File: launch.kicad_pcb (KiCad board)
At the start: 4 copper layers, 299 x 127 mm, 356 parts, among them J0 12401598E4#2A, J1 AVR-ISP-6, J2 1003-002-01100, J3 1003-002-01100, J4 12401598E4#2A, J5 12401598E4#2A, U0 USBLC6-2SC6, U1 ATmega32U4-MU, U10 AP22811AW5-7, U11 PTN5110DHQ, U12 PTN5110THQ, U13 PTN5110THQ, U14 SN74LVC1G08DCKR, U15 CBTL02043ABQ,115, U16 AP22811AW5-7‎, U17 TLV62585PDRLR, U18 LP5907MFX-3.3, U19 SN74LVC1G08DCKR, U2 USB7206, U20 AP22811AW5-7, U21 USBLC6-2SC6, U22 AP22811AW5-7, U23 AP22811AW5-7, U3 CBTL02043ABQ,115, U4 TLV62585PDRLR, U5 USBLC6-2SC6, U6 CBTL02043ABQ,115, U7 USBLC6-2SC6, U8 USBLC6-2SC6, U9 AP22811AW5-7, X1 ECS-3225MV-250-BN-TR, Y0 ECS-160-18-23G-JGN-TR

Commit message: BOM update Add manufacturer info Add key socket PN Correct USB-A to surface mount (was through hole)
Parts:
- J1: value AVR-ISP-6 -> DNP
- SWA0, SWA1, SWA2, SWA3, SWA4, SWA5, SWB0, SWB1, SWB2, SWB3, SWB4, SWB5, SWC0, SWC1, SWC2, SWC3, SWC4, SWC5, SWD0, SWD1, SWD2, SWD3, SWD4, SWD5, SWE0, SWE1, SWE2, SWE3, SWE4, SWE5, SWF0, SWF1, SWF2, SWF3, SWF4, SWF5, SWG0, SWG1, SWG2, SWG3, SWG4, SWG5, SWH0, SWH1, SWH2, SWH3, SWH4, SWH5, SWI0, SWI1, SWI2, SWI3, SWI4, SWI5, SWJ0, SWJ1, SWJ2, SWJ3, SWJ4, SWJ5, SWK0, SWK1, SWK2, SWK3, SWK4, SWK5, SWL0, SWL1, SWL2, SWL3, SWL4, SWL5, SWM0, SWM1, SWM2, SWM3, SWM4, SWM5, SWN0, SWN1, SWN2, SWN3, SWN4, SWN5: value SW_Push -> CPG151101S11
- TP1, TP2: value TestPoint -> DNP

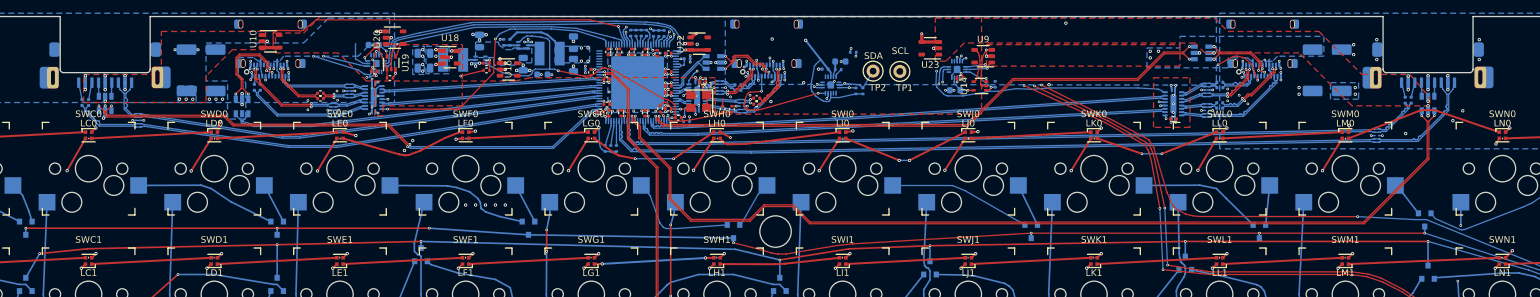
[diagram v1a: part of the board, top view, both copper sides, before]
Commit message: move USB A down 2.1 mm
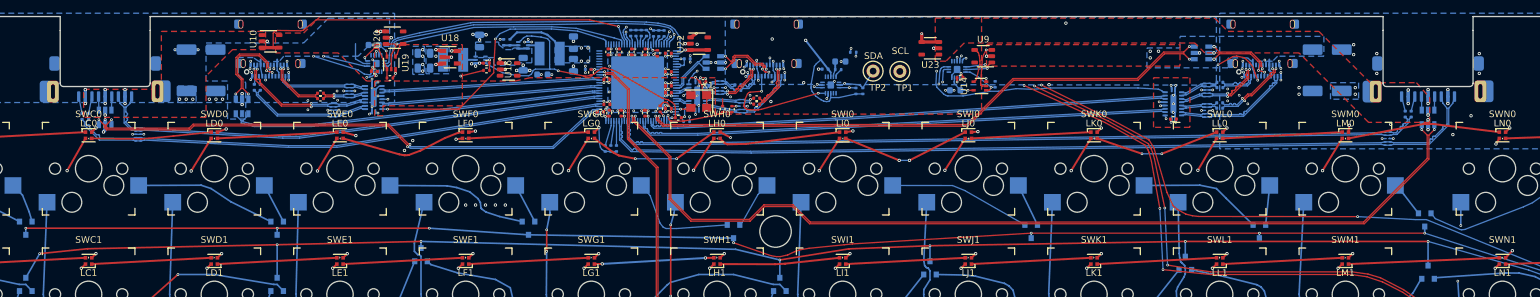
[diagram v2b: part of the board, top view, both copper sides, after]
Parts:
- moved C51 2.10 mm to (247.9, 1.75)
- moved C52 2.10 mm to (247.1, 1.75)
- moved C53 2.10 mm to (48.0, 2.10)
- moved C54 2.10 mm to (47.0, 2.10)
- moved U5 2.10 mm to (250.5, 2.25)
- moved U8 2.10 mm to (50.5, 2.25)
- moved D6 2.10 mm to (55.5, 4.80)
- moved J2 2.10 mm to (250.5, -5.90)
- moved J3 2.10 mm to (50.5, -5.90)
- moved D2 1.71 mm to (244.4, 5.45)
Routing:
- net /USB/AR_D-: track 144.7 -> 142.6 mm
- net /USB/AR_D+: track 145.6 -> 143.5 mm
- net Net-(LM0-Pad3): track 24.1 -> 23.1 mm
- net /USB/AR_RX-: track 135.4 -> 134.7 mm
- net /USB/AR_RX+: track 135.5 -> 134.7 mm
- net /USB/AR_TX-: track 123.6 -> 122.9 mm
- net /USB/AR_TX+: track 123.7 -> 123.0 mm
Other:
- outline, holes or cut-outs redrawn

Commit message: plated mounting holes adjust position of one mounting hole slightly add hole near middle.
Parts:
- added H1: MountingHole_Pad, launch:MountingHole, F.Cu at (18.9, 19.5)
- added H2: MountingHole_Pad, launch:MountingHole, F.Cu at (6.10, 105.0)
- added H3: MountingHole_Pad, launch:MountingHole, F.Cu at (30.7, 64.5)
- added H4: MountingHole_Pad, launch:MountingHole, F.Cu at (128.1, 105.0)
- added H5: MountingHole_Pad, launch:MountingHole, F.Cu at (151.9, 19.5)
- added H6: MountingHole_Pad, launch:MountingHole, F.Cu at (235.0, 105.0)
- added H7: MountingHole_Pad, launch:MountingHole, F.Cu at (273.0, 67.0)
- added H8: MountingHole_Pad, launch:MountingHole, F.Cu at (275.4, 19.5)
- added H9: MountingHole_Pad, launch:MountingHole, F.Cu at (142.0, 57.2)
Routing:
- net ROW3: track 284.0 -> 286.3 mm
- net GND: track 243.1 -> 244.0 mm, vias 277 -> 276
- net Net-(D44-Pad1): track 210.9 -> 211.4 mm
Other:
- outline, holes or cut-outs redrawn

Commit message: Adjustments for production Change laminate from ITEQ IT180A to Shengyi S1000-2     - Associated controlled impedance changes Remove circles on Cmts.User in mounting holes that were confusing manufacturer Move USB A connector SMT ground pads 0.2 mm further away from PCB edge Specify black solder mask
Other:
- net class Default: clearance 0.127 -> 0.12
- rule trace_clearance: 0.127 -> 0.12
- board text added: "Controlled impedance: Layer 1 ref layer 2, 90 ohm diff: 0.137 mm trace, 0.121 mm space Layer 4 ref layer 3, 90 ohm diff: 0.137 mm trace, 0.121 mm space"
- board text added: "Launch Rev 20200927 Board must be RoHS compliant Fabricate to IPC-A-600 Class II Material: Shengyi S1000-2 Inner copper 1 or 1/2 oz Black LPI solder mask over bare copper Vendor may remove solder mask from via holes, maximum of drill size + 3 mil Finish: OSP Silkscreen: white non conductive 100% electrical test required Remove all unused pads from inner layers All layers positive Overall thicknes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"
- board text removed: "Board must be RoHS compliant Fabricate to IPC-A-600 Class II Material: ITEQ IT180A Inner copper 1 or 1/2 oz Green LPI solder mask over bare copper Vendor may remove solder mask from via holes, maximum of drill size + 3 mil Finish: OSP Silkscreen: white non conductive 100% electrical test required Remove all unused pads from inner layers All layers positive Overall thickness: 1.6 mm +- 10 %"
- board text removed: "Controlled impedance: Layer 1 ref layer 2, 90 ohm diff: 0.122 mm trace, 0.136 mm space Layer 4 ref layer 3, 90 ohm diff: 0.122 mm trace, 0.136 mm space"
